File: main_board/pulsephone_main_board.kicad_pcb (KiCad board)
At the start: 2 copper layers, 70.5 x 128.5 mm, 27 parts, among them J1 USB_C_Receptacle_USB2.0_14P, J3 Conn_2Rows-35Pins_MountingPin, J4 Conn_2Rows-35Pins_MountingPin, J5 Conn_2Rows-35Pins_MountingPin, U1 XL1509-3.3, U2 PCM5102APWR, U5 TP4056-42-ESOP8

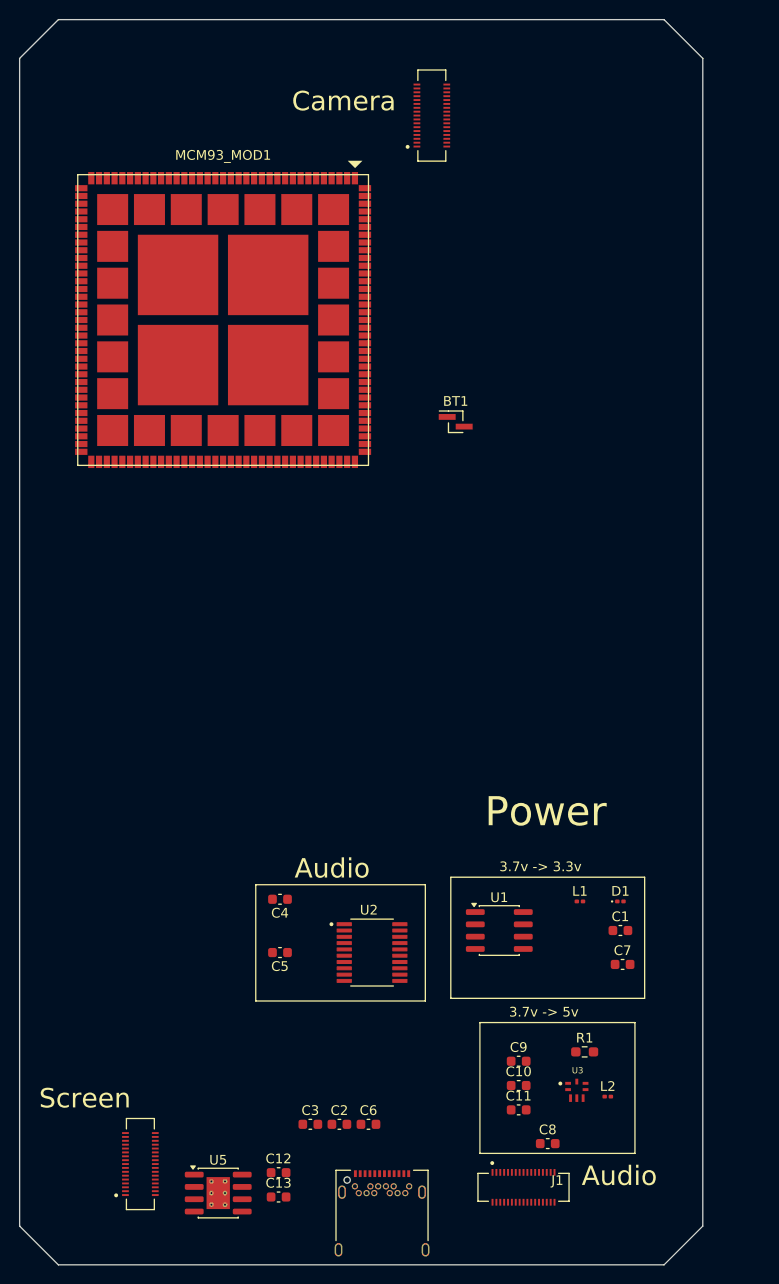
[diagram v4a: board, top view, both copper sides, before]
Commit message: High speed display traces.
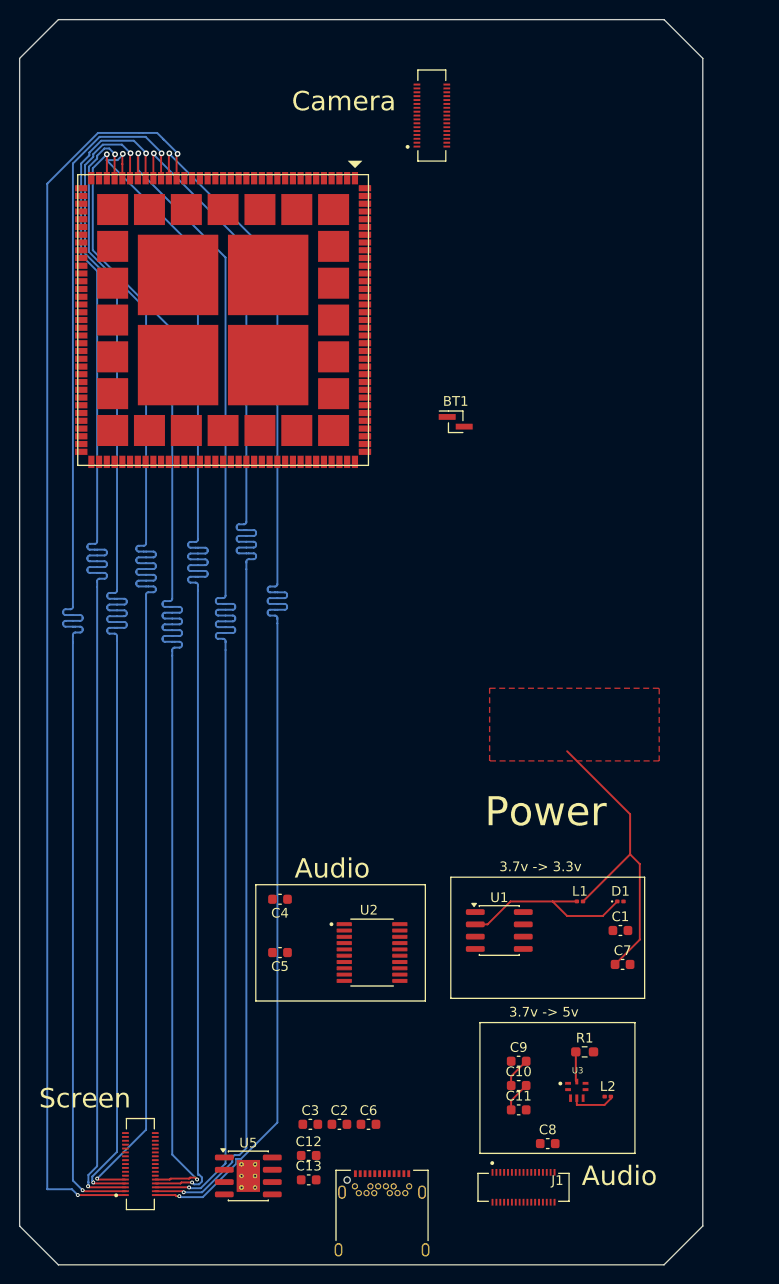
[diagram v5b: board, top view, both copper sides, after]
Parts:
- moved C12 3.57 mm to (130.8, 143.2)
- moved C13 3.57 mm to (130.8, 145.7)
- moved U5 3.57 mm to (124.6, 145.3)
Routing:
- net /DSI_D3_N: track 0.00 -> 132.3 mm, vias 0 -> 2
- net /DSI_CLK_P: track 0.00 -> 132.0 mm, vias 0 -> 2
- net /DSI_D1_N: track 0.00 -> 132.0 mm, vias 0 -> 2
- net /DSI_D3_P: track 0.00 -> 131.8 mm, vias 0 -> 2
- net /DSI_D2_N: track 0.00 -> 131.8 mm, vias 0 -> 2
- net /DSI_D2_P: track 0.00 -> 131.4 mm, vias 0 -> 2
- net /DSI_D0_N: track 0.00 -> 131.3 mm, vias 0 -> 2
- net /DSI_D0_P: track 0.00 -> 131.2 mm, vias 0 -> 2
- net /DSI_CLK_N: track 0.00 -> 131.2 mm, vias 0 -> 2
- net /DSI_D1_P: track 0.00 -> 131.1 mm, vias 0 -> 2
- net +3.3V: track 0.00 -> 33.0 mm
- net Net-(D1-K): track 0.00 -> 19.4 mm
- net Net-(U3-SW): track 0.00 -> 4.69 mm
- net Net-(C10-Pad1): track 0.00 -> 3.15 mm
- net Net-(C10-Pad2): track 0.00 -> 3.15 mm
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- added copper zone on F.Cu, net +3.3V

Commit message: Finished main_board pcb, and added branding
The next thing is to start on module development
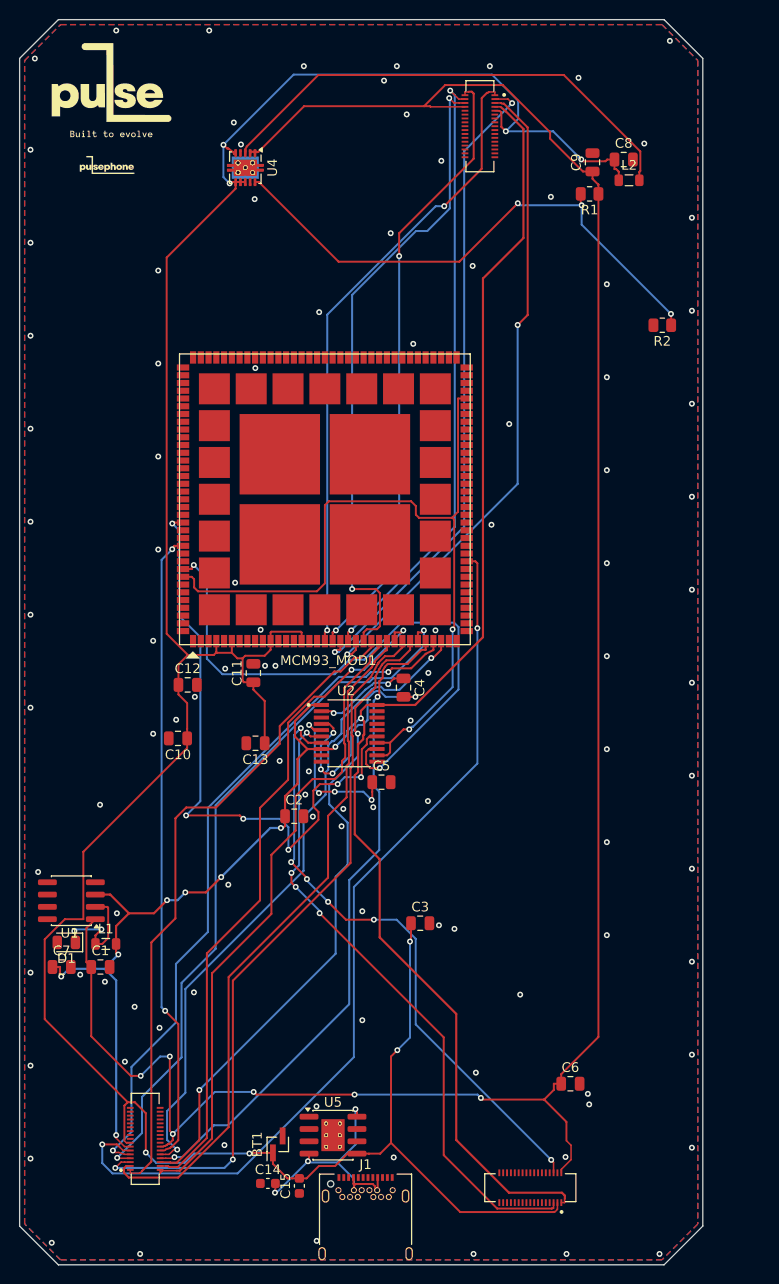
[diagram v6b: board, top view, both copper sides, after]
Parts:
- removed U3: ~, MIC2877-5.0YFT-TR:VREG_MIC2877-AYFT-TR
- added C14: 10uF, Capacitor_SMD:C_0603_1608Metric, F.Cu at (126.6, 146.1)
- added C15: 10uF, Capacitor_SMD:C_0603_1608Metric, F.Cu at (129.9, 146.4)
- added G***: LOGO, LOGO, F.Cu at (110.0, 41.0)
- added R2: 1Kohm, Resistor_SMD:R_0805_2012Metric, F.Cu at (167.3, 57.5)
- added U4: TPS61202DRC, Package_SON:Texas_S-PVSON-N10_ThermalVias, F.Cu at (124.3, 41.3)
- added nul: nul, LOGO, F.Cu at (110.5, 33.5)
- C1, C4, C5, C7: footprint Capacitor_SMD:C_0603_1608Metric -> Capacitor_SMD:C_0805_2012Metric
- C10, C11, C8, C9: value 22uF -> 20uF; footprint Capacitor_SMD:C_0603_1608Metric -> Capacitor_SMD:C_0805_2012Metric
- C12, C13, C2, C3, C6: value 10uF -> 20uF; footprint Capacitor_SMD:C_0603_1608Metric -> Capacitor_SMD:C_0805_2012Metric
- D1: footprint Diode_SMD:D_0201_0603Metric -> Diode_SMD:D_0805_2012Metric
- L1: footprint Inductor_SMD:L_0201_0603Metric -> Inductor_SMD:L_0805_2012Metric
- L2: value 1uH -> 2.2uh; footprint Inductor_SMD:L_0201_0603Metric -> Inductor_SMD:L_0805_2012Metric
- R1: value 1Mega Ohm -> 9Kohm; footprint Resistor_SMD:R_0603_1608Metric_Pad0.98x0.95mm_HandSolder -> Resistor_SMD:R_0805_2012Metric
- moved C8 101.9 mm to (163.3, 40.4)
- moved L2 94.6 mm to (163.9, 42.6)
- moved C9 93.1 mm to (160.1, 40.7), turned to 90 degrees
- moved R1 88.5 mm to (159.8, 44.0), turned to 180 degrees
- moved BT1 76.8 mm to (127.6, 142.1), turned to 90 degrees
- moved C7 57.9 mm to (105.3, 123.8)
- moved D1 57.3 mm to (105.8, 121.2), turned to 180 degrees
- moved C1 53.8 mm to (109.3, 123.8)
- moved C11 52.7 mm to (125.1, 93.4), turned to 90 degrees
- moved C10 50.2 mm to (117.3, 100.2), turned to 180 degrees
- moved C12 50.1 mm to (118.3, 94.7)
- moved L1 49.1 mm to (109.9, 121.4)
- moved C13 45.4 mm to (125.3, 100.7), turned to 180 degrees
- moved U1 44.3 mm to (106.3, 116.9), turned to 180 degrees
- moved C2 32.1 mm to (129.3, 108.2)
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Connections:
- C1 pad 1: +3.7VBAT -> +5V
- C10 pad 1: Net-(C10-Pad1) -> +3.7VBAT
- C10 pad 2: Net-(C10-Pad2) -> GND
- C11 pad 1: Net-(C10-Pad2) -> +3.7VBAT
- C12 pad 1: GND -> +3.7VBAT
- C12 pad 2: Net-(U5-CE) -> GND
- C13 pad 1: GND -> +3.7VBAT
- C13 pad 2: +3.7VBAT -> GND
- C9 pad 2: Net-(C10-Pad1) -> GND
- J5 pad 5: unconnected-(J5-Pin_5-Pad5) -> Net-(J5-Pin_5)
- J5 pad 6: unconnected-(J5-Pin_6-Pad6) -> Net-(J5-Pin_6)
- J5 pad 8: Net-(J5-Pin_8) -> unconnected-(J5-Pin_8-Pad8)
- J5 pad 9: Net-(J5-Pin_9) -> unconnected-(J5-Pin_9-Pad9)
- MCM93_MOD1 pad 11: +5V -> +3.7VBAT
- MCM93_MOD1 pad 133: /SAI_MASTERCLOCK -> /AUDIO_DATA_OUT
- MCM93_MOD1 pad 15: +5V -> +3.7VBAT
- MCM93_MOD1 pad 4: +5V -> +3.7VBAT
- MCM93_MOD1 pad 6: +5V -> +3.7VBAT
- R1 pad 1: Power Good -> +5V
- R1 pad 2: +3.7VBAT -> Net-(U4-FB)
- U1 pad 1: +3.7VBAT -> +5V
- U1 pad 4: +3.7VBAT -> unconnected-(U1-~{EN}-Pad4)
- U2 pad 12: /SAI_MASTERCLOCK -> /AUDIO_DATA_OUT
- U2 pad 6: Net-(J5-Pin_8) -> Net-(J5-Pin_5)
- U2 pad 7: Net-(J5-Pin_9) -> Net-(J5-Pin_6)
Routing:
- net +3.7VBAT: track 0.00 -> 287.0 mm, vias 0 -> 8
- net +5V: track 0.00 -> 228.8 mm, vias 0 -> 6
- net +3.3V: track 33.0 -> 218.1 mm, vias 0 -> 9
- net /I2C3_SCL: track 0.00 -> 93.9 mm, vias 0 -> 2
- net /AUDIO_DATA_OUT: track 0.00 -> 82.4 mm, vias 0 -> 2
- net /CSI_D1_N: track 0.00 -> 68.5 mm, vias 0 -> 2
- net /CSI_D0_N: track 0.00 -> 68.0 mm, vias 0 -> 2
- net /CSI_D1_P: track 0.00 -> 66.7 mm, vias 0 -> 2
- net Net-(J5-Pin_5): track 0.00 -> 66.7 mm, vias 0 -> 4
- net /I2C3_SDA: track 0.00 -> 65.8 mm, vias 0 -> 2
- net /CSI_CLK_N: track 0.00 -> 65.2 mm, vias 0 -> 2
- net /DSI_CLK_P: track 132.0 -> 67.1 mm, vias 2 -> 0
- net /AUDIO_FRAME_CLOCK: track 0.00 -> 64.9 mm, vias 0 -> 6
- net /CSI_CLK_P: track 0.00 -> 63.9 mm, vias 0 -> 2
- net Net-(J5-Pin_6): track 0.00 -> 63.8 mm, vias 0 -> 6
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- added copper zone on B.Cu, net GND
- added copper zone on F.Cu, net GND
- removed copper zone on F.Cu, net +3.3V
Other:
- board text removed: "3.7v -> 3.3v"
- board text removed: "3.7v -> 5v"
- board text removed: "Audio"
- board text removed: "Camera"
- board text removed: "Power"
- board text removed: "Screen"

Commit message: pcb: remove backup archives and reposition board logo
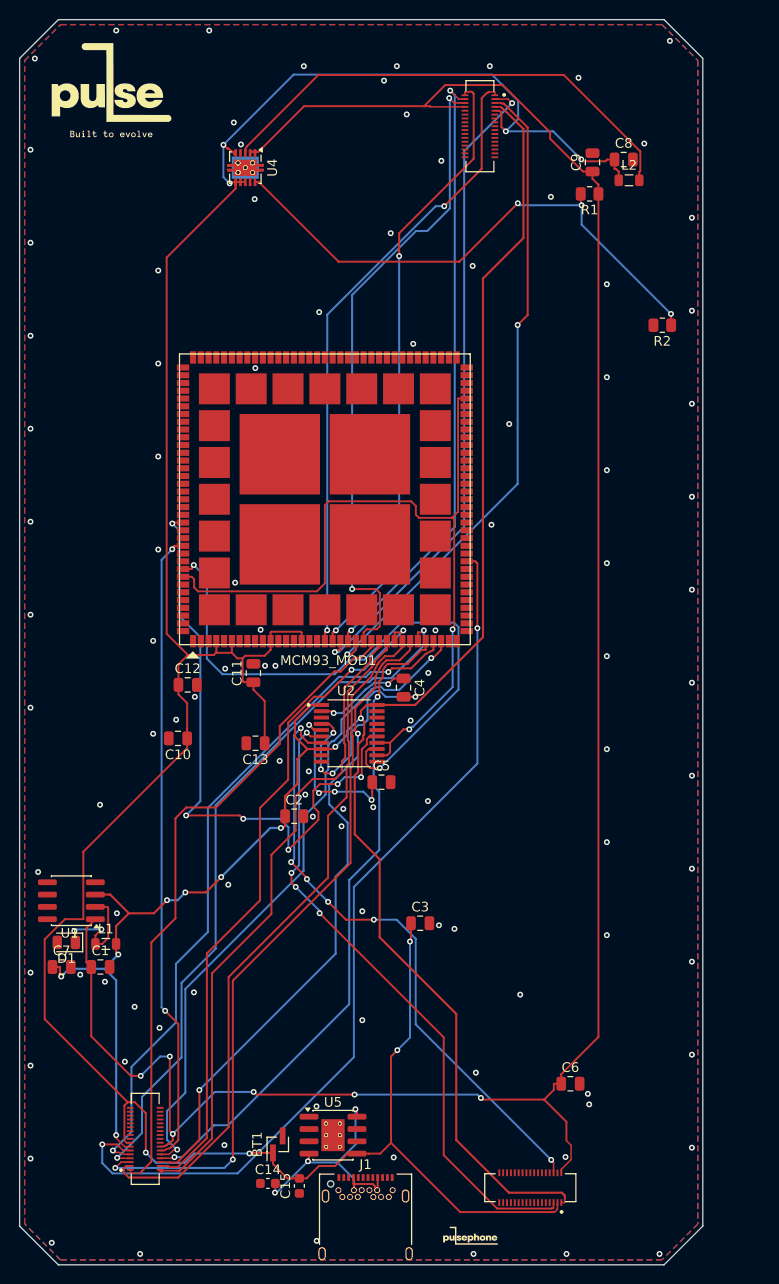
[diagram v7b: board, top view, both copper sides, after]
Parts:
- moved G*** 116.7 mm to (147.5, 151.5)
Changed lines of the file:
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@@
 	(footprint "LOGO"
 		(layer "F.Cu")
-		(at 110 41)
+		(at 147.5 151.5)
 		(property "Reference" "G***"
 			(at 0 0 0)

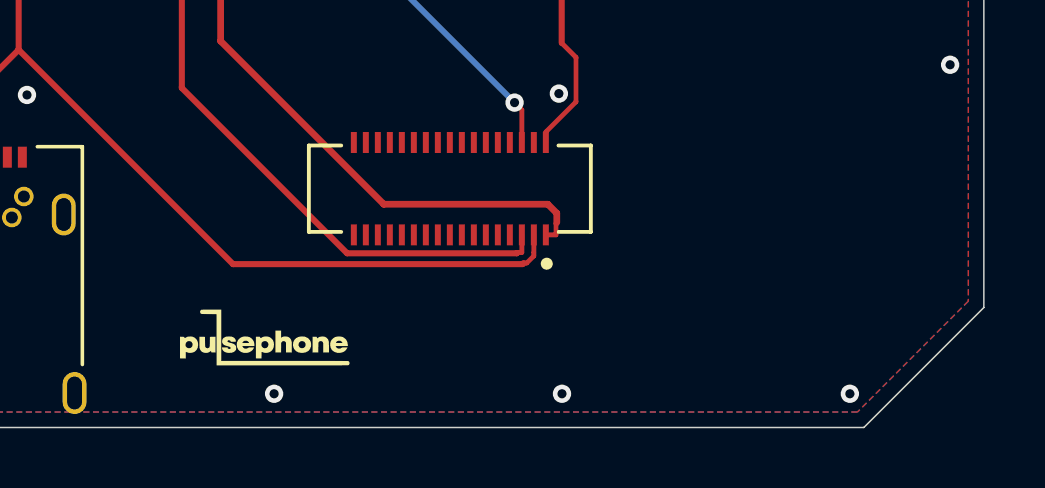
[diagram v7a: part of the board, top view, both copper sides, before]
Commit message: pcb: update board design and related project files
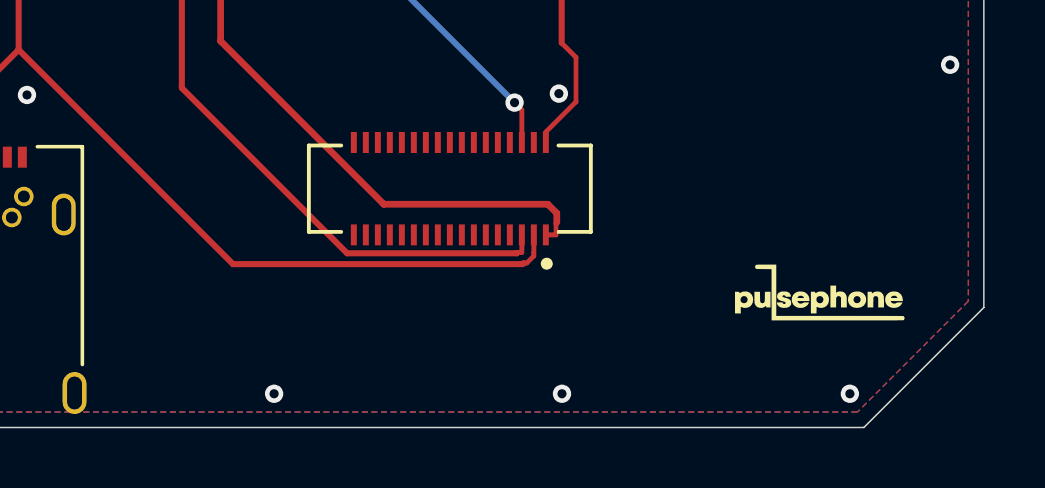
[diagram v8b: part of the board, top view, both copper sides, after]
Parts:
- moved G*** 18.6 mm to (166.0, 150.0)
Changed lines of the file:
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@@
 	(footprint "LOGO"
 		(layer "F.Cu")
-		(at 147.5 151.5)
+		(at 166 150)
 		(property "Reference" "G***"
 			(at 0 0 0)
